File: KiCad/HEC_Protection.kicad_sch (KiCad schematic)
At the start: 20 parts, among them U11 74LS00, U11 74LS32, U12 74LS04, U16 74LS32, U17 74LS74, U18 74LS138, U18 74LS74, U19 74LS30, U22 74LS02, U23 74LS74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

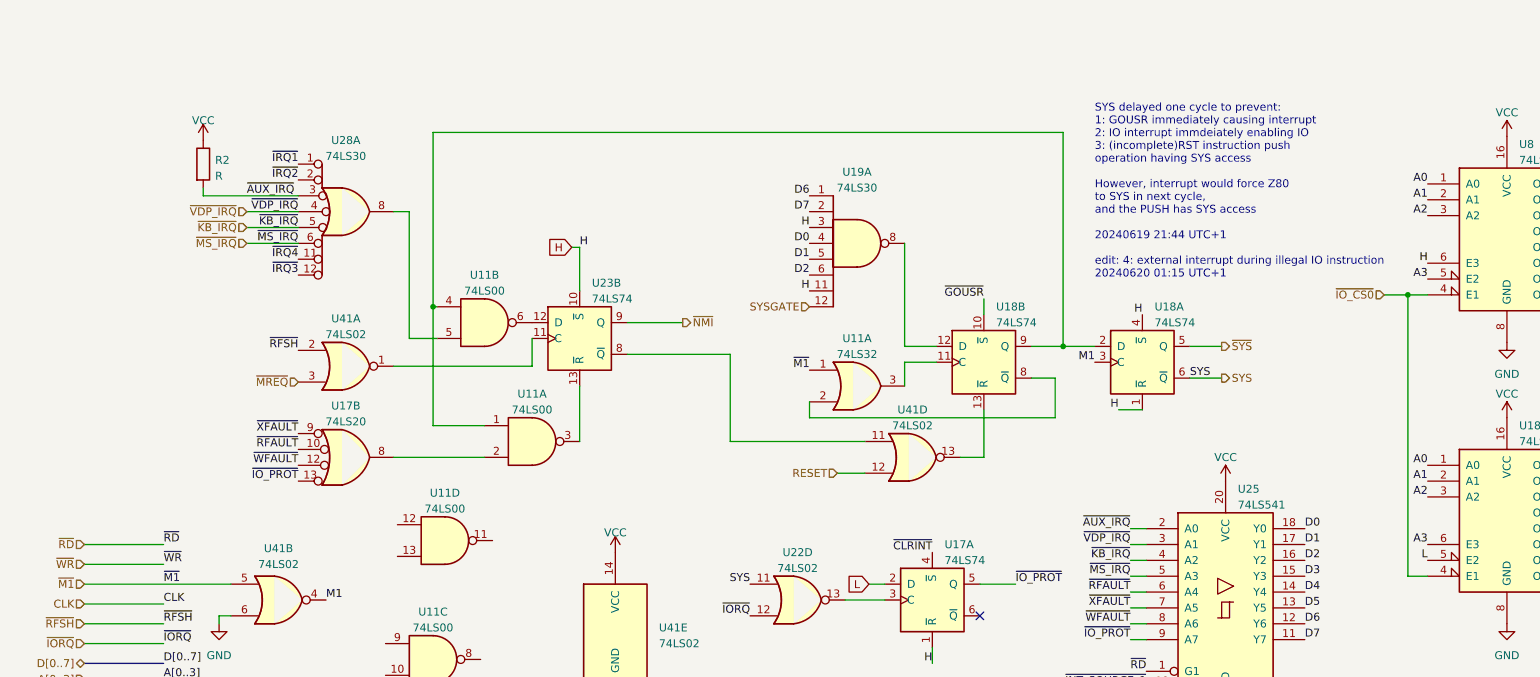
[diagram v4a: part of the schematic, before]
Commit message: Add I2C bus
Change audio pins on the bus to carry I2C signal. This can be used for configuring onboard devices such as RGB to HDMI converters, sound mixers, GPIOs, etc.
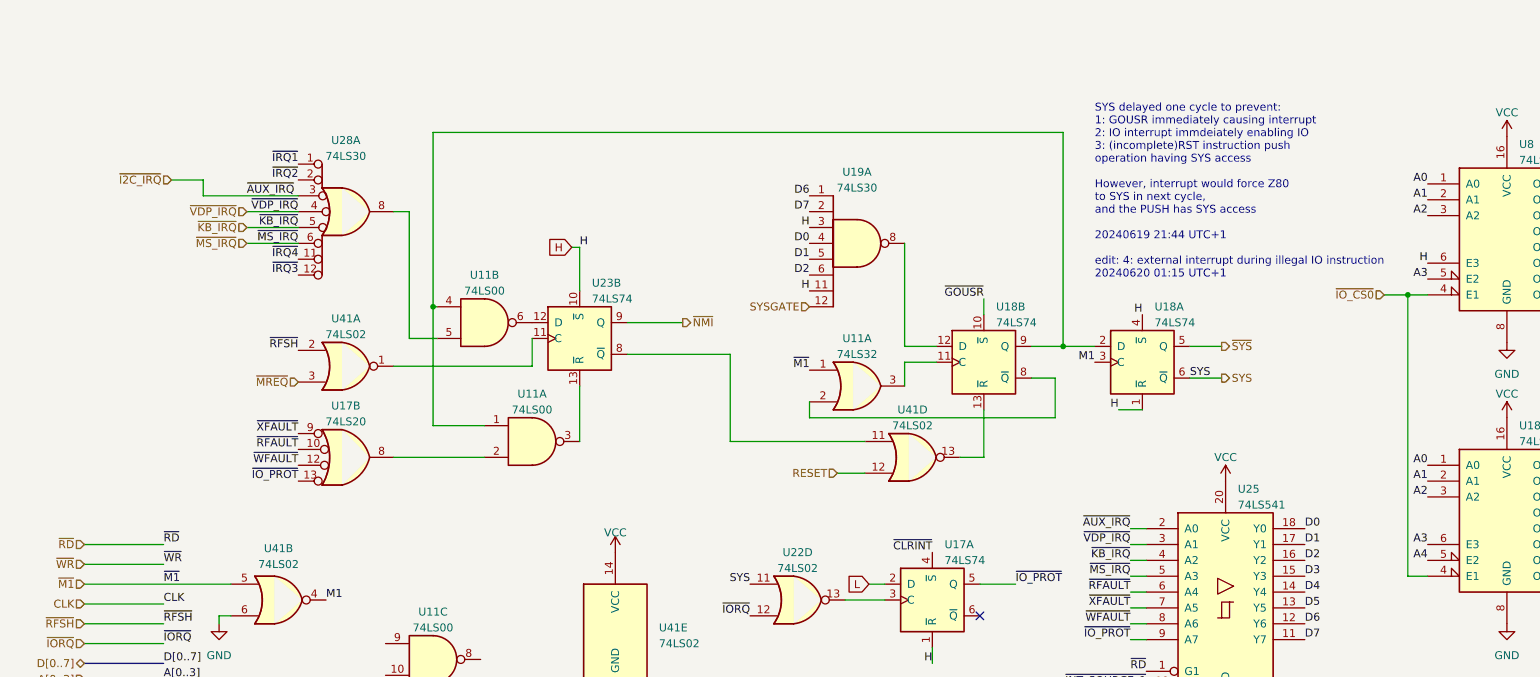
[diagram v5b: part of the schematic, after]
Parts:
- removed R2: R, Resistor_THT:R_Axial_DIN0207_L6.3mm_D2.5mm_P7.62mm_Horizontal, symbol Device:R
- removed unit 4 of U11
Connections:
- net L: no longer U18.5 (E2)
- net ~{AUX_IRQ} renamed ~{I2C_IRQ}
- new net A4: U18.5 (E2)
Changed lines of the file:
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@@
+    (stroke (width 0) (type default))
+  )
+  (wire (pts (xy 36.195 26.67) (xy 41.275 26.67))
     (stroke (width 0) (type default))
   )
@@
     (stroke (width 0) (type default))
   )
-  (wire (pts (xy 41.275 27.94) (xy 41.275 29.21))
+  (wire (pts (xy 41.275 26.67) (xy 41.275 29.21))
     (stroke (width 0) (type default))
   )
@@
     (effects (font (size 1.27 1.27)) (justify right bottom))
   )
+  (label "A4" (at 237.49 87.63 180) (fields_autoplaced)
+    (effects (font (size 1.27 1.27)) (justify right bottom))
+  )
   (label "~{XFAULT}" (at 189.865 95.25 180) (fields_autoplaced)
     (effects (font (size 1.27 1.27)) (justify right bottom))
@@
   )
   (label "H" (at 80.01 153.67 180) (fields_autoplaced)
-    (effects (font (size 1.27 1.27)) (justify right bottom))
-  )
-  (label "L" (at 237.49 87.63 180) (fields_autoplaced)
     (effects (font (size 1.27 1.27)) (justify right bottom))
   )
@@
   (hierarchical_label "~{IOPORT_H}" (shape output) (at 265.43 74.93 0) (fields_autoplaced)
     (effects (font (size 1.27 1.27)) (justify left))
+  )
+  (hierarchical_label "~{I2C_IRQ}" (shape input) (at 36.195 26.67 180) (fields_autoplaced)
+    (effects (font (size 1.27 1.27)) (justify right))
   )
   (hierarchical_label "SYS" (shape output) (at 204.47 58.42 0) (fields_autoplaced)
@@
     )
   )
-  (symbol (lib_id "power:VCC") (at 41.275 20.32 0) (unit 1)
-    (in_bom yes) (on_board yes) (dnp no) (fields_autoplaced)
-    (property "Reference" "#PWR0111" (at 41.275 24.13 0)
-      (effects (font (size 1.27 1.27)) hide)
-    )
-    (property "Value" "VCC" (at 41.275 17.145 0)
-      (effects (font (size 1.27 1.27)))
-    )
-    (property "Footprint" "" (at 41.275 20.32 0)
-      (effects (font (size 1.27 1.27)) hide)
-    )
-    (property "Datasheet" "" (at 41.275 20.32 0)
-      (effects (font (size 1.27 1.27)) hide)
-    )
-    (pin "1")
-    (instances
-      (project "HEC1"
-        (path "/87935374-b60a-4f41-99da-94b76103dd77/2930b625-d6a3-4a7f-9d41-a454efcef99d"
-          (reference "#PWR0111") (unit 1)
-        )
-      )
-    )
-  )
   (symbol (lib_id "power:VCC") (at 59.69 161.29 0) (unit 1)
     (in_bom yes) (on_board yes) (dnp no) (fields_autoplaced)
@@
         )
       )
-    )
-  )
-  (symbol (lib_id "Device:R") (at 41.275 24.13 0) (unit 1)
-    (in_bom yes) (on_board yes) (dnp no) (fields_autoplaced)
-    (property "Reference" "R2" (at 43.18 23.495 0)
-      (effects (font (size 1.27 1.27)) (justify left))
-    )
-    (property "Value" "R" (at 43.18 26.035 0)
-      (effects (font (size 1.27 1.27)) (justify left))
-    )
-    (property "Footprint" "Resistor_THT:R_Axial_DIN0207_L6.3mm_D2.5mm_P7.62mm_Horizontal" (at 39.497 24.13 90)
-      (effects (font (size 1.27 1.27)) hide)
-    )
-    (property "Datasheet" "~" (at 41.275 24.13 0)
-      (effects (font (size 1.27 1.27)) hide)
-    )
-    (pin "1")
-    (pin "2")
-    (instances
-      (project "HEC1"
-        (path "/87935374-b60a-4f41-99da-94b76103dd77/2930b625-d6a3-4a7f-9d41-a454efcef99d"
-          (reference "R2") (unit 1)
-        )
-      )
-    )
-  )
-  (symbol (lib_id "74xx:74LS00") (at 80.01 84.455 0) (unit 4)
-    (in_bom yes) (on_board yes) (dnp no) (fields_autoplaced)
-    (property "Reference" "U11" (at 80.0017 76.835 0)
-      (effects (font (size 1.27 1.27)))
-    )
-    (property "Value" "74LS00" (at 80.0017 79.375 0)
-      (effects (font (size 1.27 1.27)))
-    )
-    (property "Footprint" "Library:DIP-14_W7.62mm_Socket_ThinPads" (at 80.01 84.455 0)
-      (effects (font (size 1.27 1.27)) hide)
-    )
-    (property "Datasheet" "http://www.ti.com/lit/gpn/sn74ls00" (at 80.01 84.455 0)
-      (effects (font (size 1.27 1.27)) hide)
-    )
-    (pin "1")
-    (pin "2")
-    (pin "3")
-    (pin "4")
-    (pin "5")
-    (pin "6")
-    (pin "10")
-    (pin "8")
-    (pin "9")
-    (pin "11")
-    (pin "12")
-    (pin "13")
-    (pin "14")
-    (pin "7")
-    (instances
-      (project "HEC1"
-        (path "/87935374-b60a-4f41-99da-94b76103dd77/2930b625-d6a3-4a7f-9d41-a454efcef99d"
-          (reference "U11") (unit 4)
-        )
-      )

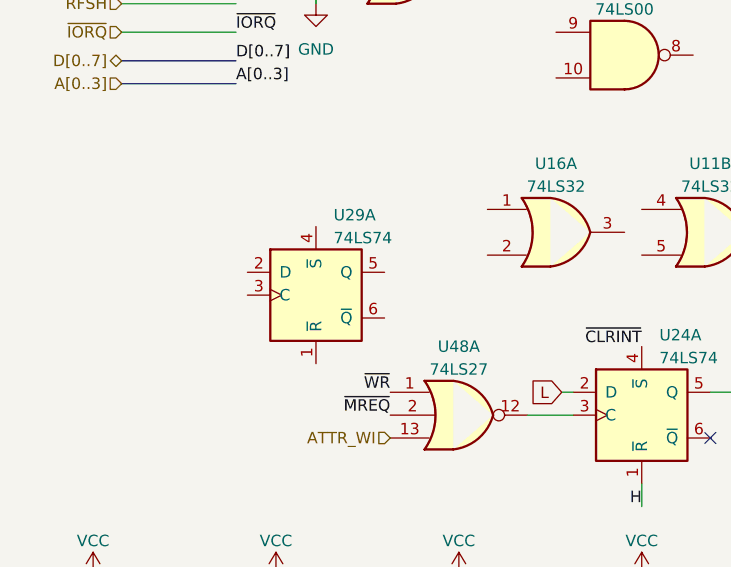
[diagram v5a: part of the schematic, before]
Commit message: Fancy power circuit
Added a circuit to switch power, short press to power on, long press to power off.
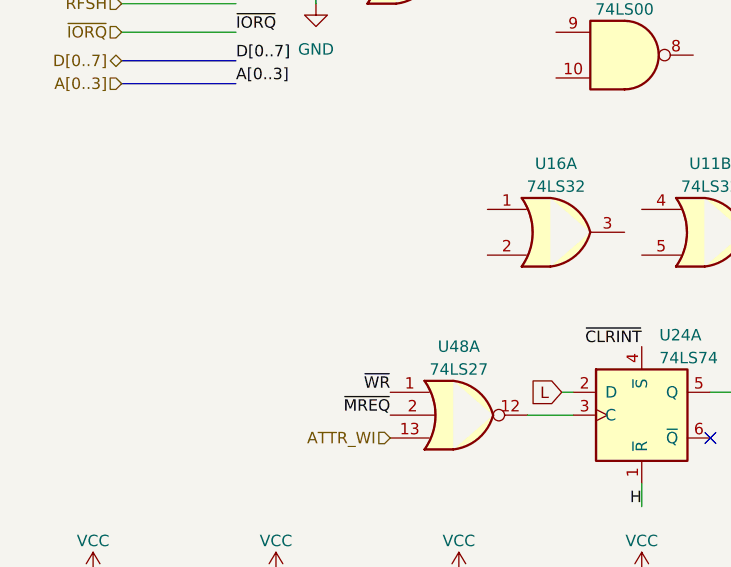
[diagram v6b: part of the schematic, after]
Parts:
- removed unit 1 of U29
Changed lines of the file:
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@@
-    )
-  )
-  (symbol (lib_id "74xx:74LS74") (at 43.815 130.175 0) (unit 1)
-    (in_bom yes) (on_board yes) (dnp no) (fields_autoplaced)
-    (property "Reference" "U29" (at 45.7709 121.285 0)
-      (effects (font (size 1.27 1.27)) (justify left))
-    )
-    (property "Value" "74LS74" (at 45.7709 123.825 0)
-      (effects (font (size 1.27 1.27)) (justify left))
-    )
-    (property "Footprint" "Library:DIP-14_W7.62mm_Socket_ThinPads" (at 43.815 130.175 0)
-      (effects (font (size 1.27 1.27)) hide)
-    )
-    (property "Datasheet" "74xx/74hc_hct74.pdf" (at 43.815 130.175 0)
-      (effects (font (size 1.27 1.27)) hide)
-    )
-    (pin "1")
-    (pin "2")
-    (pin "3")
-    (pin "4")
-    (pin "5")
-    (pin "6")
-    (pin "10")
-    (pin "11")
-    (pin "12")
-    (pin "13")
-    (pin "8")
-    (pin "9")
-    (pin "14")
-    (pin "7")
-    (instances
-      (project "HEC1"
-        (path "/87935374-b60a-4f41-99da-94b76103dd77/2930b625-d6a3-4a7f-9d41-a454efcef99d"
-          (reference "U29") (unit 1)
-        )
-      )
     )
   )

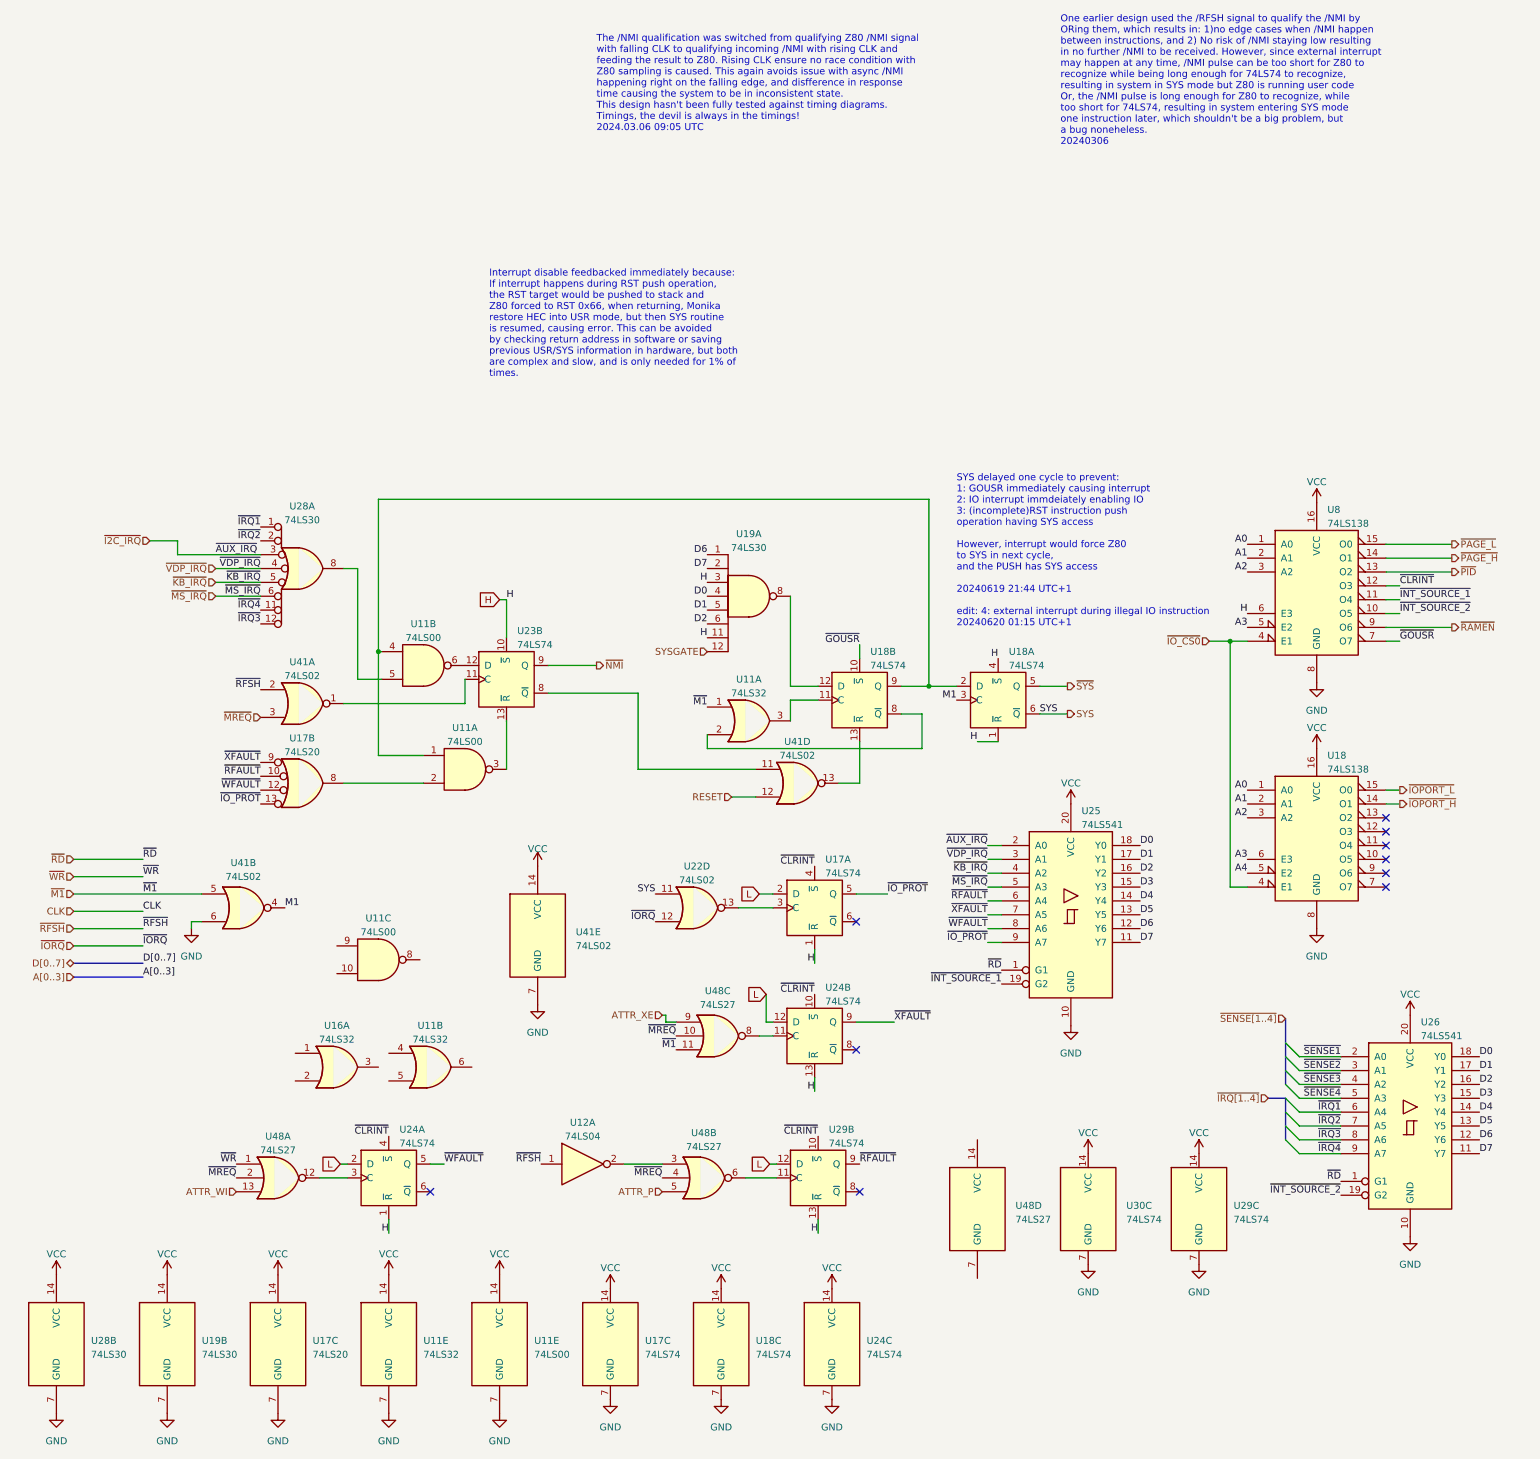
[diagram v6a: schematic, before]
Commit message: Spamming Net-ties
Spam Net-ties everywhere, replacing old H and L symbols in preparation for a 4-layber board design.
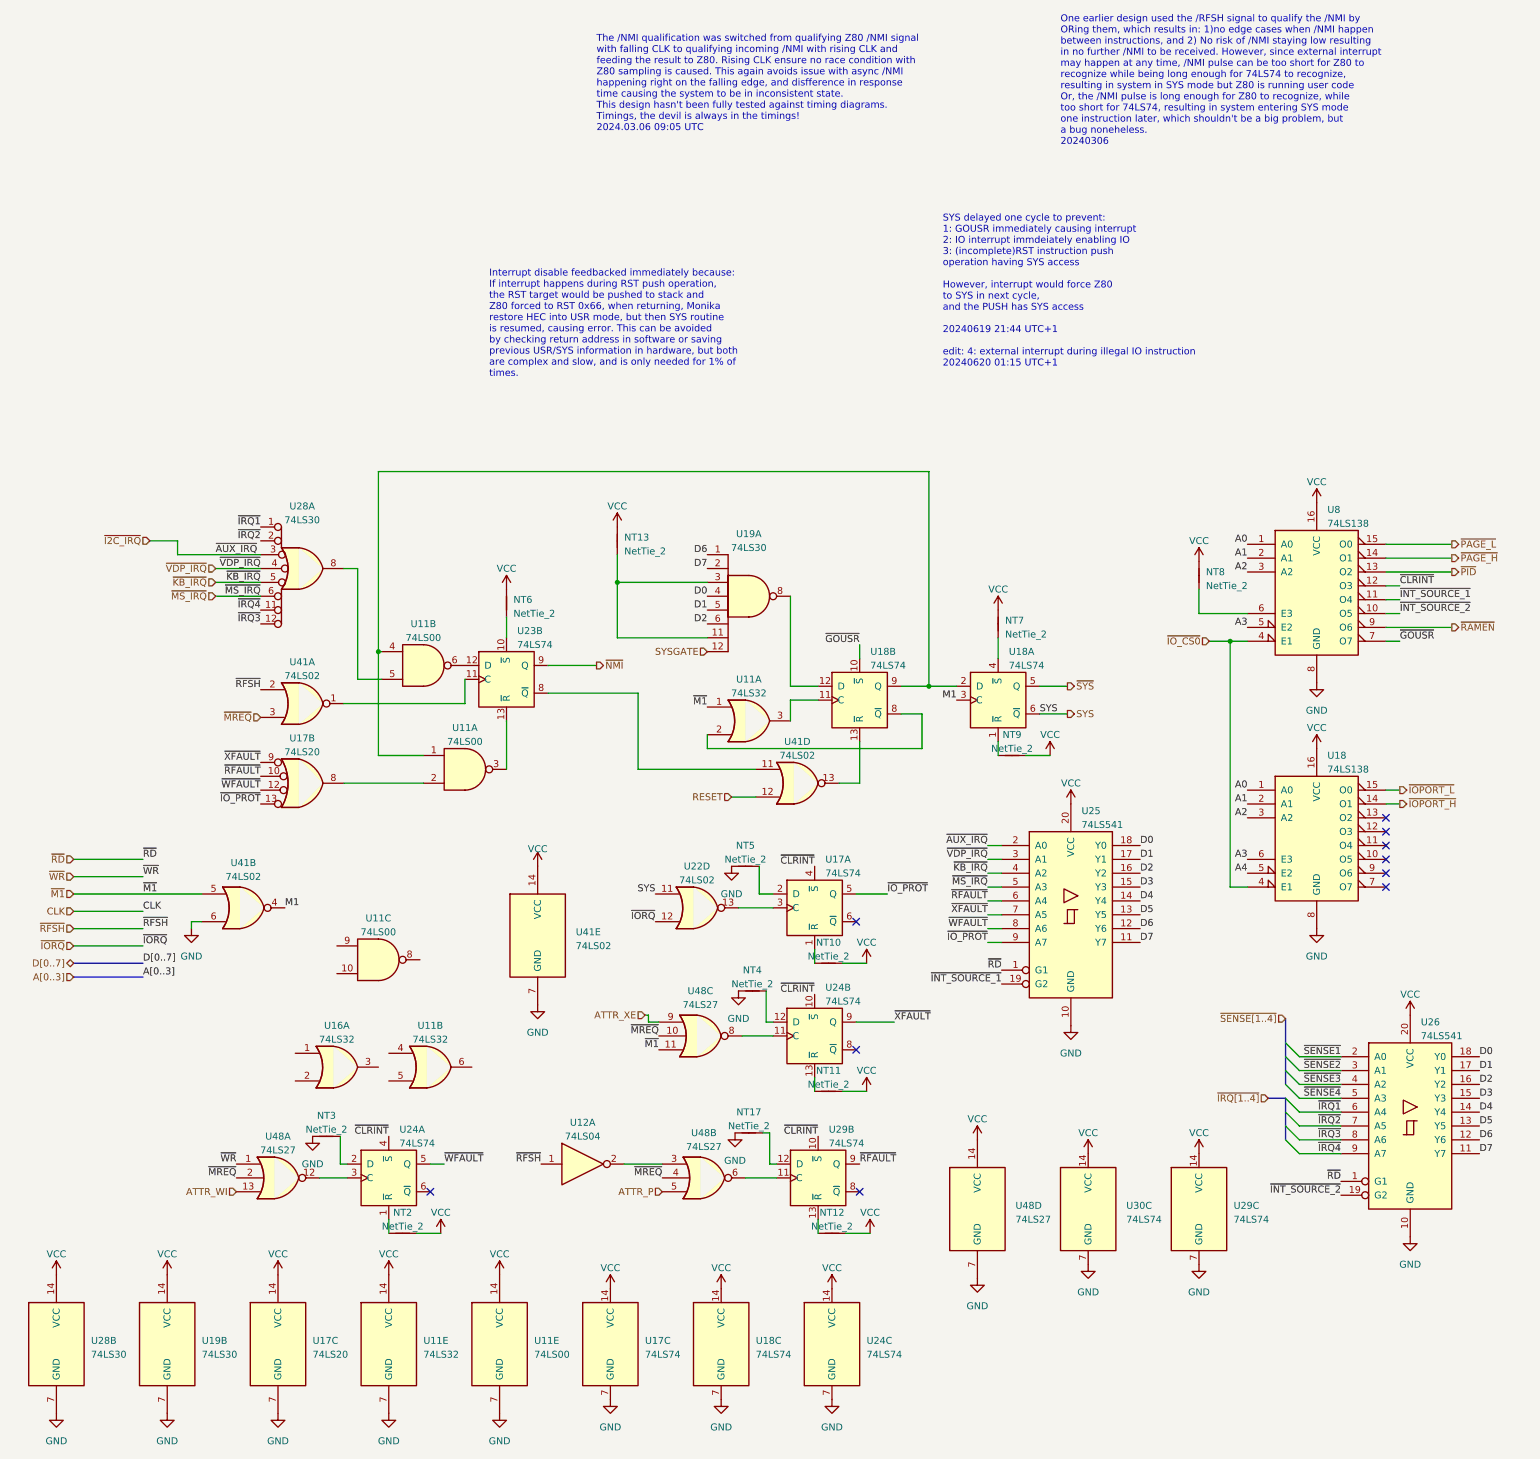
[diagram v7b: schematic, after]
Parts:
- added NT10, NT11, NT12, NT13, NT17, NT2, NT3, NT4, NT5, NT6, NT7, NT8, NT9: NetTie_2, symbol Device:NetTie_2
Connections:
- net GND: now also U48.7 (GND), NT17.1, NT3.1, NT4.1, NT5.1
- net VCC: now also U48.14 (VCC), NT10.2, NT11.2, NT12.2, NT13.2, NT2.2, NT6.2, NT7.2, NT8.2, NT9.2
- removed net H: U17.1 (~{R}), U18.1 (~{R}), U18.4 (~{S}), U19.11, U19.3, U23.10 (~{S}), U24.1 (~{R}), U24.13 (~{R}), U29.13 (~{R}), U8.6 (E3)
- removed net L: U17.2 (D), U24.12 (D), U24.2 (D), U29.12 (D)
- new net: NT17.2, U29.12 (D)
- new net: NT12.1, U29.13 (~{R})
- new net: NT6.1, U23.10 (~{S})
- new net: NT9.1, U18.1 (~{R})
- new net: NT13.1, U19.11, U19.3
- new net: NT11.1, U24.13 (~{R})
- new net: NT4.2, U24.12 (D)
- new net: NT7.1, U18.4 (~{S})
- new net: NT8.1, U8.6 (E3)
- new net: NT5.2, U17.2 (D)
- new net: NT10.1, U17.1 (~{R})
- new net: NT2.1, U24.1 (~{R})
- new net: NT3.2, U24.2 (D)
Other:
- moved on the sheet: U48C
